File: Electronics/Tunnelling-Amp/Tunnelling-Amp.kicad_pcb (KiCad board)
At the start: 2 copper layers, 50 x 20 mm, 19 parts, among them J1 RF_Shield_Two_Pieces, U1 ADA4627-1

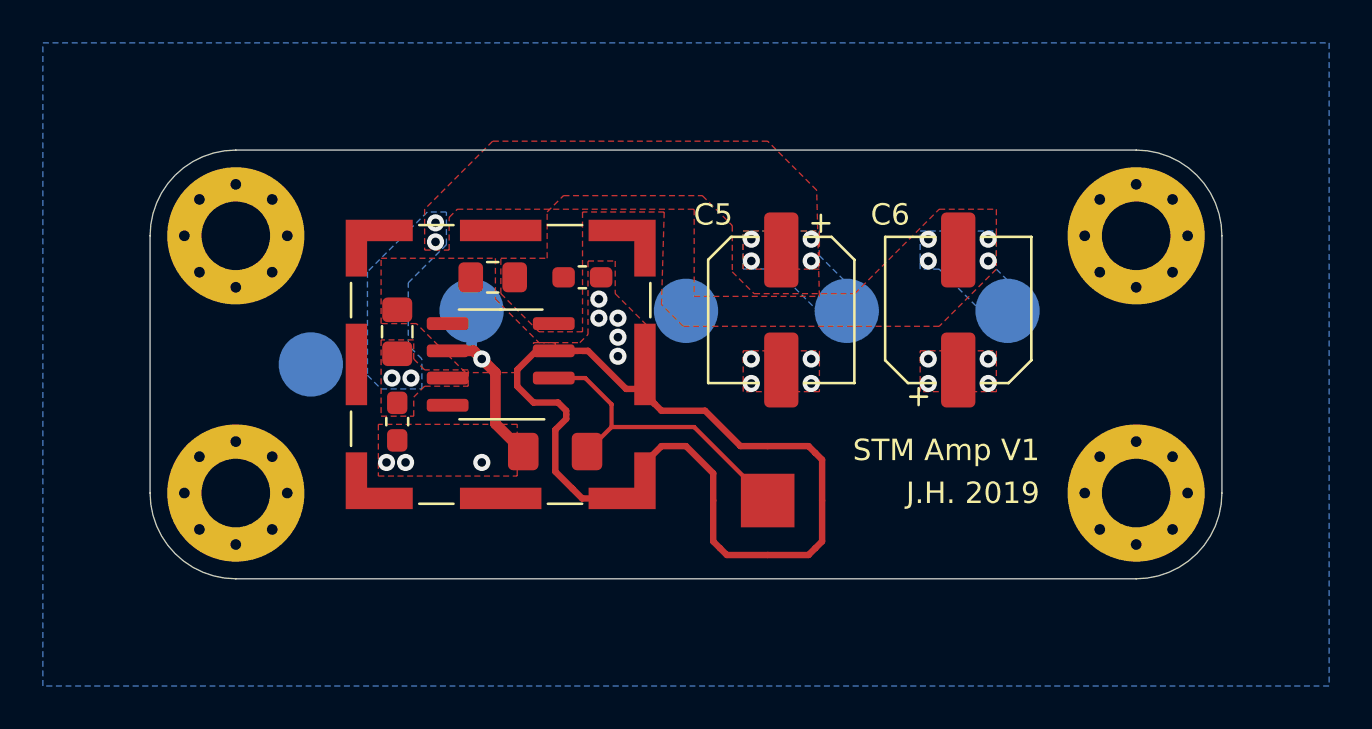
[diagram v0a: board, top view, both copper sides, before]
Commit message: Supply board and tunneling amp finished
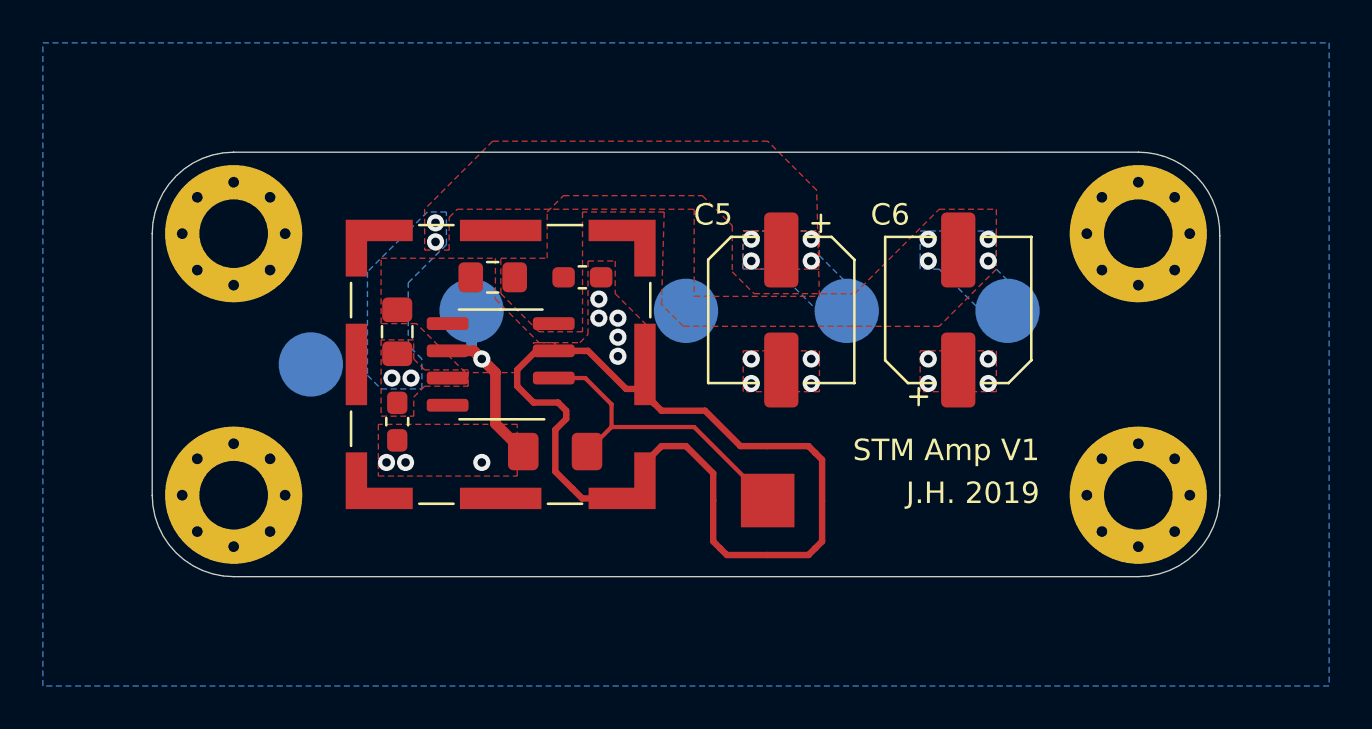
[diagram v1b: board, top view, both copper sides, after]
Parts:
- moved REF** 0.14 mm to (91.3, 131.2)
- moved REF** 0.14 mm to (91.3, 119.0)
- moved REF** 0.14 mm to (133.5, 119.0)
- moved REF** 0.14 mm to (133.5, 131.2)
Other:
- board size 50 x 20 mm -> 49.8 x 19.8 mm
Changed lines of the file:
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@@
-(kicad_pcb (version 20171130) (host pcbnew 5.1.2)
+(kicad_pcb (version 20171130) (host pcbnew 5.1.4)
   (general
     (thickness 1.6)
@@
   )
   (setup
-    (last_trace_width 0.5)
+    (last_trace_width 0.2)
     (user_trace_width 0.2)
     (user_trace_width 0.3)
@@
   )
   (module MountingHole:MountingHole_3.2mm_M3_Pad_Via (layer F.Cu)
-    (at 133.4 119.115)
+    (at 133.5 119.015)
     (descr "Mounting Hole 3.2mm, M3")
     (tags "mounting hole 3.2mm m3")
@@
   )
   (module MountingHole:MountingHole_3.2mm_M3_Pad_Via (layer F.Cu)
-    (at 133.4 131.115)
+    (at 133.5 131.215)
     (descr "Mounting Hole 3.2mm, M3")
     (tags "mounting hole 3.2mm m3")
@@
   )
   (module MountingHole:MountingHole_3.2mm_M3_Pad_Via (layer F.Cu)
-    (at 91.4 131.115)
+    (at 91.3 131.215)
     (descr "Mounting Hole 3.2mm, M3")
     (tags "mounting hole 3.2mm m3")
@@
   )
   (module MountingHole:MountingHole_3.2mm_M3_Pad_Via (layer F.Cu)
-    (at 91.4 119.115)
+    (at 91.3 119.015)
     (descr "Mounting Hole 3.2mm, M3")
     (tags "mounting hole 3.2mm m3")
@@
   )
   (gr_poly (pts (xy 118.115 134.005) (xy 118.75 133.37) (xy 118.75 129.56) (xy 118.115 128.925) (xy 114.94 128.925) (xy 113.289 127.274) (xy 111.257 127.274) (xy 110.241 126.258) (xy 109.606 126.258) (xy 107.828 124.48) (xy 105.415 124.48) (xy 104.526 125.369) (xy 104.526 126.131) (xy 105.288 126.893) (xy 106.431 126.893) (xy 106.812 127.274) (xy 106.812 127.655) (xy 106.304 128.163) (xy 106.304 130.068) (xy 107.574 131.338) (xy 110.495 131.338) (xy 110.495 129.687) (xy 111.257 128.925) (xy 112.4 128.925) (xy 113.67 130.195) (xy 113.67 133.37) (xy 114.305 134.005)) (layer F.Mask) (width 0.4))
-  (gr_line (start 137.4 131.115) (end 137.4 119.115) (layer Edge.Cuts) (width 0.05))
-  (gr_line (start 91.4 135.115) (end 133.4 135.115) (layer Edge.Cuts) (width 0.05))
-  (gr_line (start 87.4 119.115) (end 87.4 131.115) (layer Edge.Cuts) (width 0.05))
-  (gr_line (start 133.4 115.115) (end 91.4 115.115) (layer Edge.Cuts) (width 0.05))
-  (gr_arc (start 133.4 131.115) (end 133.4 135.115) (angle -90) (layer Edge.Cuts) (width 0.05))
-  (gr_arc (start 133.4 119.115) (end 137.4 119.115) (angle -90) (layer Edge.Cuts) (width 0.05))
-  (gr_arc (start 91.4 119.115) (end 91.4 115.115) (angle -90) (layer Edge.Cuts) (width 0.05))
-  (gr_arc (start 91.4 131.115) (end 87.4 131.115) (angle -90) (layer Edge.Cuts) (width 0.05))
+  (gr_line (start 137.3 131.215) (end 137.3 119.115) (layer Edge.Cuts) (width 0.05))
+  (gr_line (start 91.3 135.015) (end 133.5 135.015) (layer Edge.Cuts) (width 0.05))
+  (gr_line (start 87.5 119.015) (end 87.5 131.215) (layer Edge.Cuts) (width 0.05))
+  (gr_line (start 133.5 115.213684) (end 91.3 115.215) (layer Edge.Cuts) (width 0.05))
+  (gr_arc (start 133.5 131.215) (end 133.5 135.015) (angle -90) (layer Edge.Cuts) (width 0.05))
+  (gr_arc (start 133.5 119.015) (end 137.3 119.115) (angle -91.50743576) (layer Edge.Cuts) (width 0.05))
+  (gr_arc (start 91.3 119.015) (end 91.3 115.215) (angle -90) (layer Edge.Cuts) (width 0.05))
+  (gr_arc (start 91.3 131.215) (end 87.5 131.215) (angle -90) (layer Edge.Cuts) (width 0.05))
   (segment (start 114.94 128.925) (end 113.289 127.274) (width 0.3) (layer F.Cu) (net 1))
   (segment (start 118.75 129.56) (end 118.4325 129.2425) (width 0.3) (layer F.Cu) (net 1))
@@
   (via (at 118.242 126.004) (size 0.8) (drill 0.4) (layers F.Cu B.Cu) (net 1))
   (via (at 118.242 124.861) (size 0.8) (drill 0.4) (layers F.Cu B.Cu) (net 1))
-  (via (at 108.336 122.067) (size 0.8) (drill 0.4) (layers F.Cu B.Cu) (net 1) (status 1000000))
-  (via (at 126.497 120.289) (size 0.8) (drill 0.4) (layers F.Cu B.Cu) (net 3))
-  (via (at 126.497 119.273) (size 0.8) (drill 0.4) (layers F.Cu B.Cu) (net 3))
+  (via (at 108.336 122.067) (size 0.8) (drill 0.4) (layers F.Cu B.Cu) (net 1))
   (via (at 99.573 125.75) (size 0.8) (drill 0.4) (layers F.Cu B.Cu) (net 2))
   (via (at 98.684 125.75) (size 0.8) (drill 0.4) (layers F.Cu B.Cu) (net 2))
   (via (at 100.716 119.4) (size 0.8) (drill 0.4) (layers F.Cu B.Cu) (net 2))
   (via (at 100.716 118.511) (size 0.8) (drill 0.4) (layers F.Cu B.Cu) (net 2))
-  (via (at 123.703 119.273) (size 0.8) (drill 0.4) (layers F.Cu B.Cu) (net 3))
-  (via (at 123.703 120.289) (size 0.8) (drill 0.4) (layers F.Cu B.Cu) (net 3))
   (via (at 118.242 120.289) (size 0.8) (drill 0.4) (layers F.Cu B.Cu) (net 2))
   (via (at 115.448 120.289) (size 0.8) (drill 0.4) (layers F.Cu B.Cu) (net 2))
   (via (at 115.448 119.273) (size 0.8) (drill 0.4) (layers F.Cu B.Cu) (net 2))
   (via (at 118.242 119.273) (size 0.8) (drill 0.4) (layers F.Cu B.Cu) (net 2))
+  (via (at 126.497 120.289) (size 0.8) (drill 0.4) (layers F.Cu B.Cu) (net 3))
+  (via (at 126.497 119.273) (size 0.8) (drill 0.4) (layers F.Cu B.Cu) (net 3))
+  (via (at 123.703 119.273) (size 0.8) (drill 0.4) (layers F.Cu B.Cu) (net 3))
+  (via (at 123.703 120.289) (size 0.8) (drill 0.4) (layers F.Cu B.Cu) (net 3))
   (segment (start 108.9265 128.036) (end 107.7835 129.179) (width 0.2) (layer F.Cu) (net 4))
   (segment (start 116.21 131.465) (end 112.781 128.036) (width 0.2) (layer F.Cu) (net 4))

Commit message: Fixed values in schematic
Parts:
- C1, C2: value 10n -> 47n
- C5, C6: value CP -> 22u
- U1: value ADA4627-1 -> ADA4637-1
